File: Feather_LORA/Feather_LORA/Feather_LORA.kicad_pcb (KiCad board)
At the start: 2 copper layers, 100 x 100 mm, 7 parts, among them J1 Conn_01x04_Female, J2 Conn_01x02_Male, J3 Conn_01x06_Male, J4 Conn_01x06_Male, J5 Conn_01x06_Male, U1 FGPMMOPA6H_GPS, U2 Feather32u4RFM95

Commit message: Adding better pad clearances. IDK why there are the rings round all of my pads. Need to get rid of that.
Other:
- net class Default: clearance 0.2 -> 0.1524; trace_width 0.25 -> 0.1524; via_dia 0.8 -> 0.6858; via_drill 0.4 -> 0.3302
- rule pad_to_mask_clearance: 0.051 -> 0.0508
- rule trace_clearance: 0.2 -> 0.1524
- rule trace_min: 0.2 -> 0.1524
- rule via_min_drill: 0.3 -> 0.254
- rule via_min_size: 0.4 -> 0.508
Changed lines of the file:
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@@
   )
   (setup
-    (last_trace_width 0.25)
-    (trace_clearance 0.2)
+    (last_trace_width 0.1524)
+    (trace_clearance 0.1524)
     (zone_clearance 0.508)
     (zone_45_only no)
-    (trace_min 0.2)
+    (trace_min 0.1524)
     (segment_width 0.2)
     (edge_width 0.15)
-    (via_size 0.8)
-    (via_drill 0.4)
-    (via_min_size 0.4)
-    (via_min_drill 0.3)
+    (via_size 0.6858)
+    (via_drill 0.3302)
+    (via_min_size 0.508)
+    (via_min_drill 0.254)
     (uvia_size 0.3)
     (uvia_drill 0.1)
@@
     (pad_size 1.524 1.524)
     (pad_drill 0.762)
-    (pad_to_mask_clearance 0.051)
+    (pad_to_mask_clearance 0.0508)
     (solder_mask_min_width 0.25)
     (aux_axis_origin 0 0)
@@
   (net 13 "Net-(J3-Pad6)")
   (net_class Default "This is the default net class."
-    (clearance 0.2)
-    (trace_width 0.25)
-    (via_dia 0.8)
-    (via_drill 0.4)
+    (clearance 0.1524)
+    (trace_width 0.1524)
+    (via_dia 0.6858)
+    (via_drill 0.3302)
     (uvia_dia 0.3)
     (uvia_drill 0.1)
+    (diff_pair_gap 1)
+    (diff_pair_width 0.2)
     (add_net +3V3)
     (add_net GND)
@@
     (descr "Molex Micro-Fit 3.0 Connector System, 43650-0400 (compatible alternatives: 43650-0401, 43650-0402), 4 Pins per row (https://www.molex.com/pdm_docs/sd/436500300_sd.pdf), generated with kicad-footprint-generator")
     (tags "connector Molex Micro-Fit_3.0 top entry")
+    (clearance 0.4)
     (fp_text reference J1 (at 4.5 -10.12) (layer F.SilkS)
       (effects (font (size 1 1) (thickness 0.15)))
@@
   (module Adafruit:AdafruitFeather (layer F.Cu)
     (at 176.022 111.252)
+    (clearance 0.37)
     (fp_text reference U2 (at -2.54 -2.04) (layer F.SilkS)
       (effects (font (size 1 1) (thickness 0.15)))
@@
     (descr "Through hole straight pin header, 1x02, 2.54mm pitch, single row")
     (tags "Through hole pin header THT 1x02 2.54mm single row")
+    (clearance 0.37)
     (fp_text reference J2 (at 0 -2.33 180) (layer F.SilkS)
       (effects (font (size 1 1) (thickness 0.15)))
@@
     (descr "Through hole straight pin header, 1x06, 2.54mm pitch, single row")
     (tags "Through hole pin header THT 1x06 2.54mm single row")
+    (solder_paste_margin -0.2)
+    (clearance 0.35)
     (fp_text reference J3 (at 0 -2.33 180) (layer F.SilkS)
       (effects (font (size 1 1) (thickness 0.15)))
@@
     (descr "Through hole straight pin header, 1x06, 2.54mm pitch, single row")
     (tags "Through hole pin header THT 1x06 2.54mm single row")
+    (clearance 0.35)
     (fp_text reference J4 (at 0 -2.33) (layer F.SilkS)
       (effects (font (size 1 1) (thickness 0.15)))
@@
     (descr "Through hole straight pin header, 1x06, 2.54mm pitch, single row")
     (tags "Through hole pin header THT 1x06 2.54mm single row")
+    (clearance 0.35)
     (fp_text reference J5 (at 0 -2.33) (layer F.SilkS)
       (effects (font (size 1 1) (thickness 0.15)))

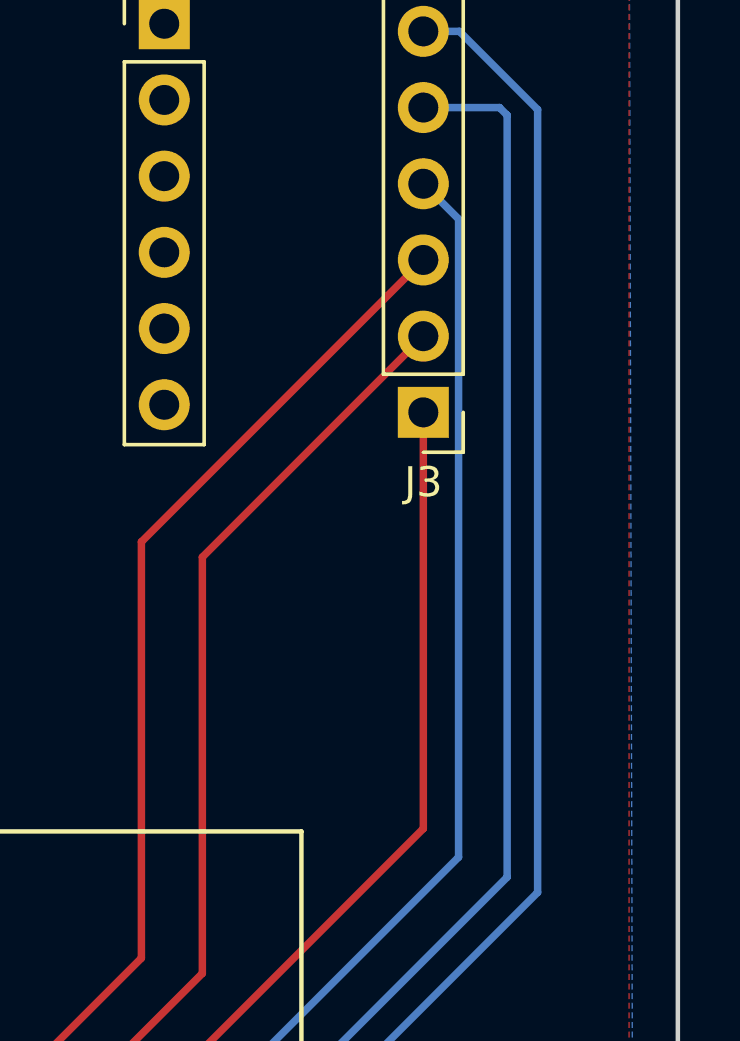
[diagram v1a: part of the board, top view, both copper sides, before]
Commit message: fixed clearnce problem
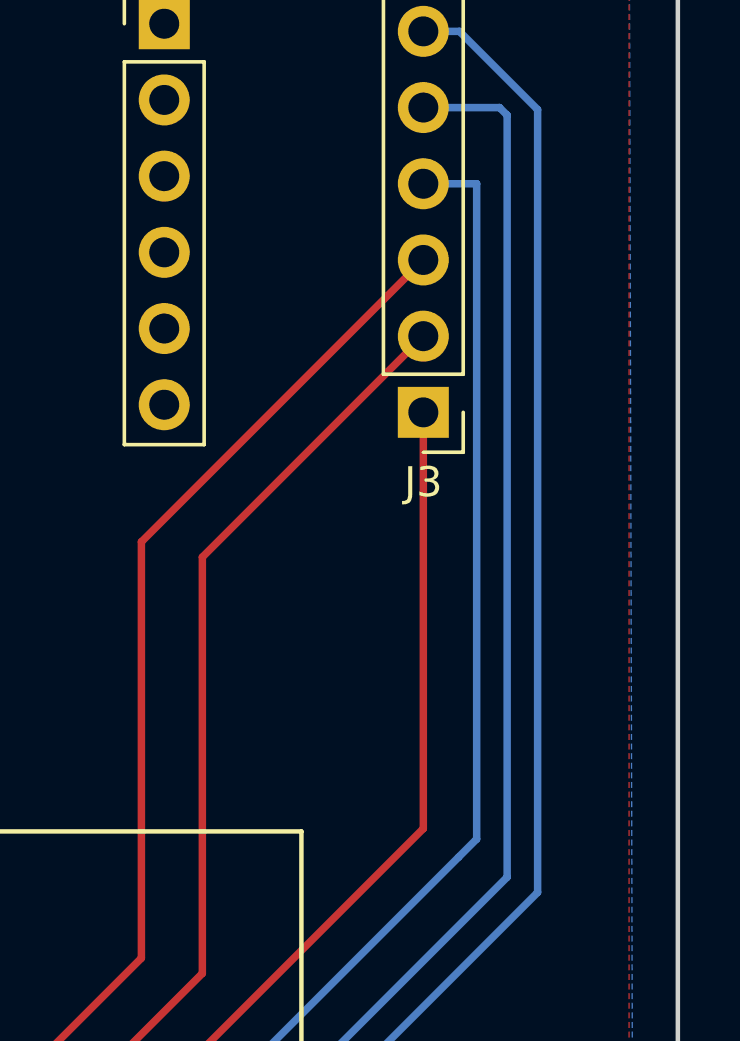
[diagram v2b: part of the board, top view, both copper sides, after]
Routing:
- net Net-(J3-Pad4): track 76.3 -> 77.9 mm
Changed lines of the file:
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@@
     (thickness 1.6)
     (drawings 4)
-    (tracks 57)
+    (tracks 58)
     (zones 0)
     (modules 7)
@@
   (segment (start 182.118 76.2) (end 191.516 66.802) (width 0.25) (layer F.Cu) (net 10))
   (segment (start 182.118 90.075608) (end 182.118 76.2) (width 0.25) (layer F.Cu) (net 10))
-  (segment (start 192.691001 65.437001) (end 192.691001 86.708999) (width 0.25) (layer B.Cu) (net 11))
-  (segment (start 191.516 64.262) (end 192.691001 65.437001) (width 0.25) (layer B.Cu) (net 11))
   (segment (start 192.691001 86.708999) (end 172.974 106.426) (width 0.25) (layer B.Cu) (net 11))
   (segment (start 172.974 113.367389) (end 186.115081 126.50847) (width 0.25) (layer B.Cu) (net 11))
   (segment (start 172.974 106.426) (end 172.974 113.367389) (width 0.25) (layer B.Cu) (net 11))
+  (segment (start 191.516 64.262) (end 193.294 64.262) (width 0.25) (layer B.Cu) (net 11))
+  (segment (start 193.294 86.106) (end 192.691001 86.708999) (width 0.25) (layer B.Cu) (net 11))
+  (segment (start 193.294 64.262) (end 193.294 86.106) (width 0.25) (layer B.Cu) (net 11))
   (segment (start 186.115081 123.96847) (end 175.006 112.859389) (width 0.25) (layer B.Cu) (net 12))
   (segment (start 175.006 112.859389) (end 175.006 106.68) (width 0.25) (layer B.Cu) (net 12))

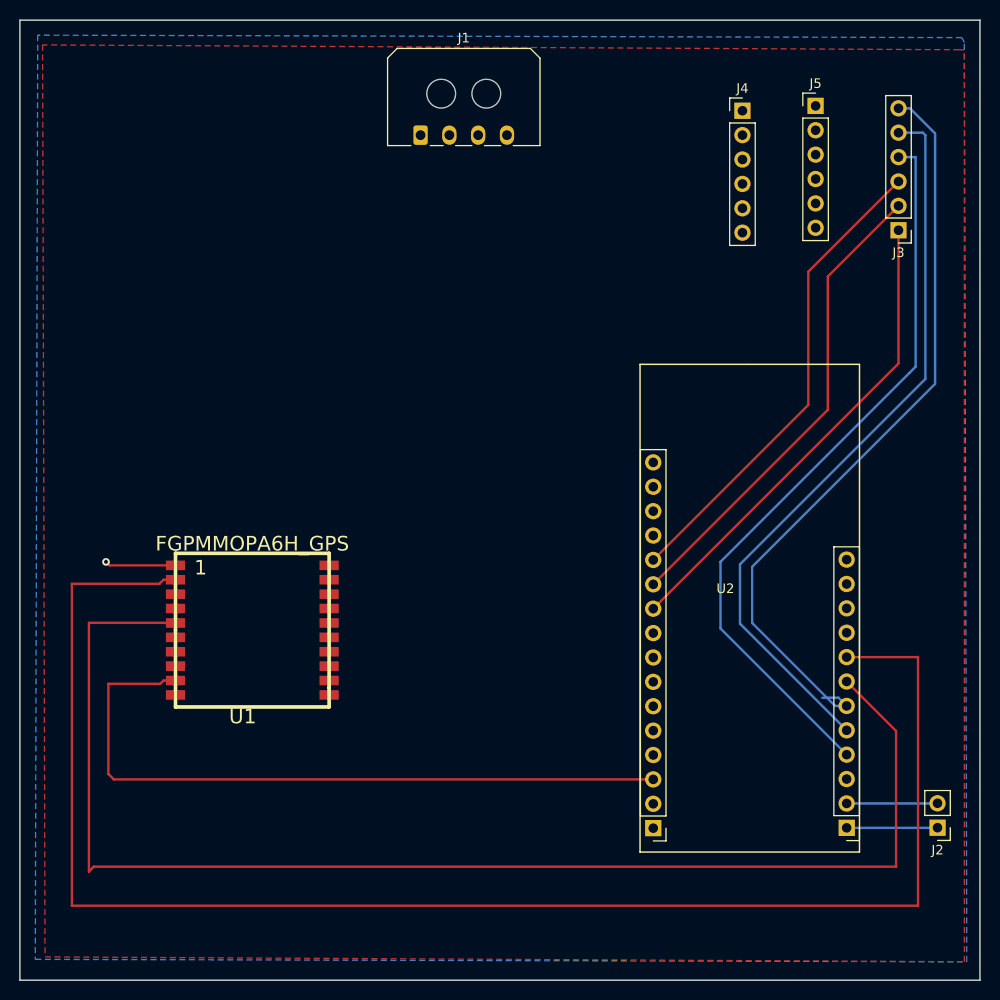
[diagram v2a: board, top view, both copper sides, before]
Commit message: Added sma and U.FL connectors for the ant
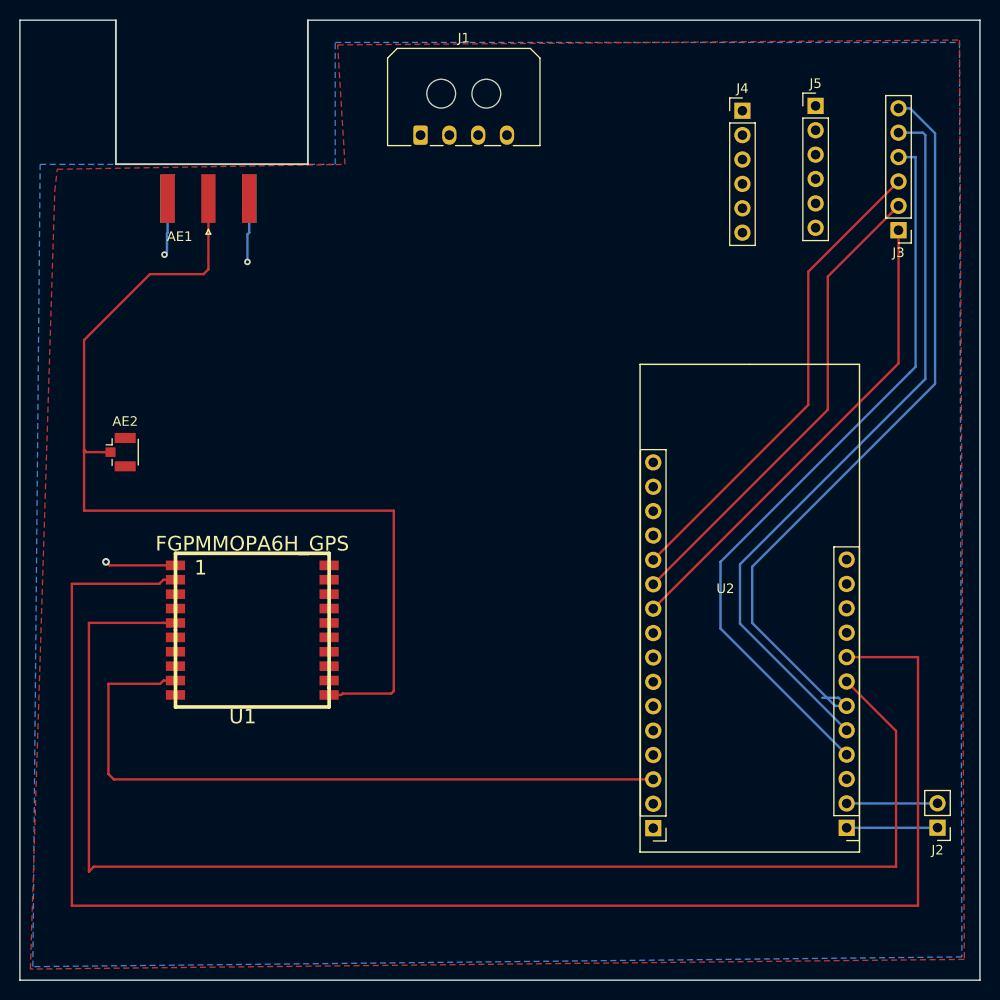
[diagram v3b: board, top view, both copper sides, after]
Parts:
- added AE1: Antenna_Shield, Connector_Coaxial:SMA_Amphenol_132289_EdgeMount, F.Cu at (119.6, 68.6)
- added AE2: Antenna_Shield, Connector_Coaxial:U.FL_Hirose_U.FL-R-SMT-1_Vertical, F.Cu at (110.5, 95.0)
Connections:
- U1 pad 11: (no net) -> Net-(AE1-Pad1)
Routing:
- net Net-(AE1-Pad1): track 0.00 -> 101.5 mm
- net GND: track 0.00 -> 11.1 mm, vias 0 -> 2
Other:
- outline, holes or cut-outs redrawn
- net class Default: trace_width 0.1524 -> 0.25

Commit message: Fixing for minimizing ant trace lenght. Added silk screen for pin mapping.
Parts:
- moved U1 28.1 mm to (114.0, 87.4), turned to 90 degrees
- moved AE2 22.1 mm to (126.2, 79.5)
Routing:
- net Net-(AE1-Pad1): track 101.5 -> 15.7 mm
- net Net-(U1-Pad2): track 166.0 -> 137.4 mm
- net Net-(U1-Pad5): track 140.6 -> 121.9 mm
- net Net-(U1-Pad9): track 73.5 -> 62.9 mm
- net +3V3: track 7.39 -> 4.24 mm
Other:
- board text added: "A0"
- board text added: "A1"
- board text added: "A2"
- board text added: "D10"
- board text added: "D6"
- board text added: "D9"
- board text added: "SCL"
- board text added: "SDA"

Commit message: fixed to do terminal blocks
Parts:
- J3, J4, J5: footprint Connector_PinHeader_2.54mm:PinHeader_1x06_P2.54mm_Vertical -> TerminalBlock_TE-Connectivity:TerminalBlock_TE_282834-6_1x06_P2.54mm_Horizontal
- moved J4 15.8 mm to (159.8, 56.1)
- moved J3 5.18 mm to (192.5, 77.0), turned to 90 degrees
- moved J5 3.78 mm to (180.3, 56.1)
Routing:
- net Net-(J3-Pad6): track 80.1 -> 72.5 mm
- net Net-(J3-Pad4): track 77.9 -> 72.3 mm
- net Net-(J3-Pad5): track 77.5 -> 72.6 mm
- net Net-(J3-Pad1): track 50.0 -> 45.3 mm
- net Net-(J3-Pad2): track 50.0 -> 48.9 mm
- net Net-(J3-Pad3): track 50.0 -> 49.0 mm
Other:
- board text added: "3.3v"
- board text added: "GND"
